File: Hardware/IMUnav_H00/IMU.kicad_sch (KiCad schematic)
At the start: 11 parts, among them U10 ADIS16505-2BMLZ, U8 MPU-6050, U9 LSM303C

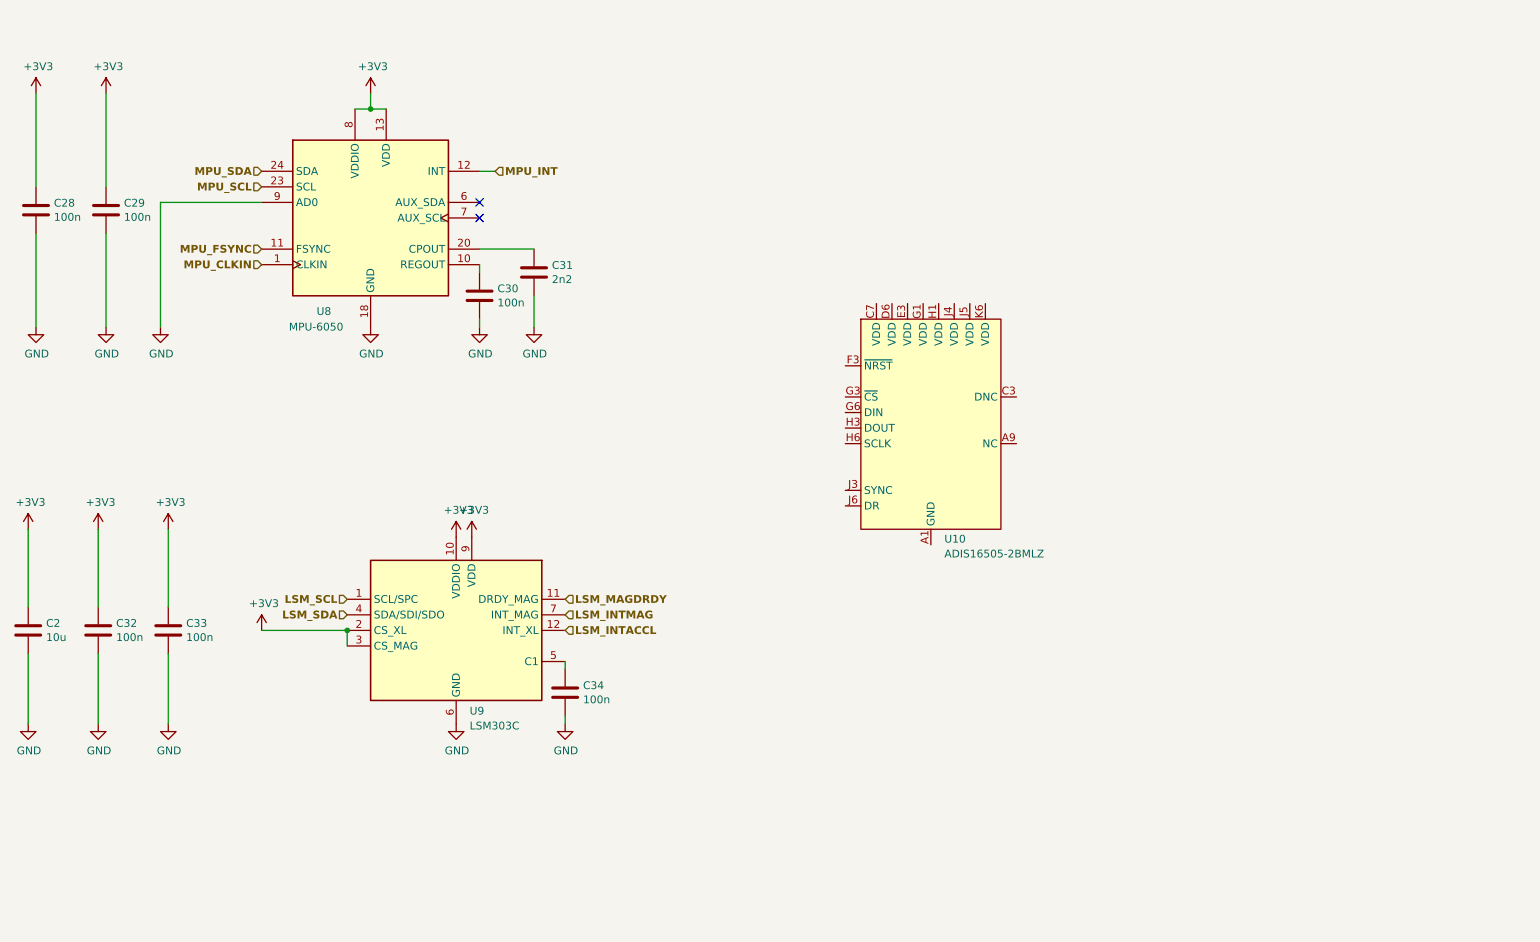
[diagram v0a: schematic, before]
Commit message: Added IMU connection, created symbol for ADIS16505 PCB version
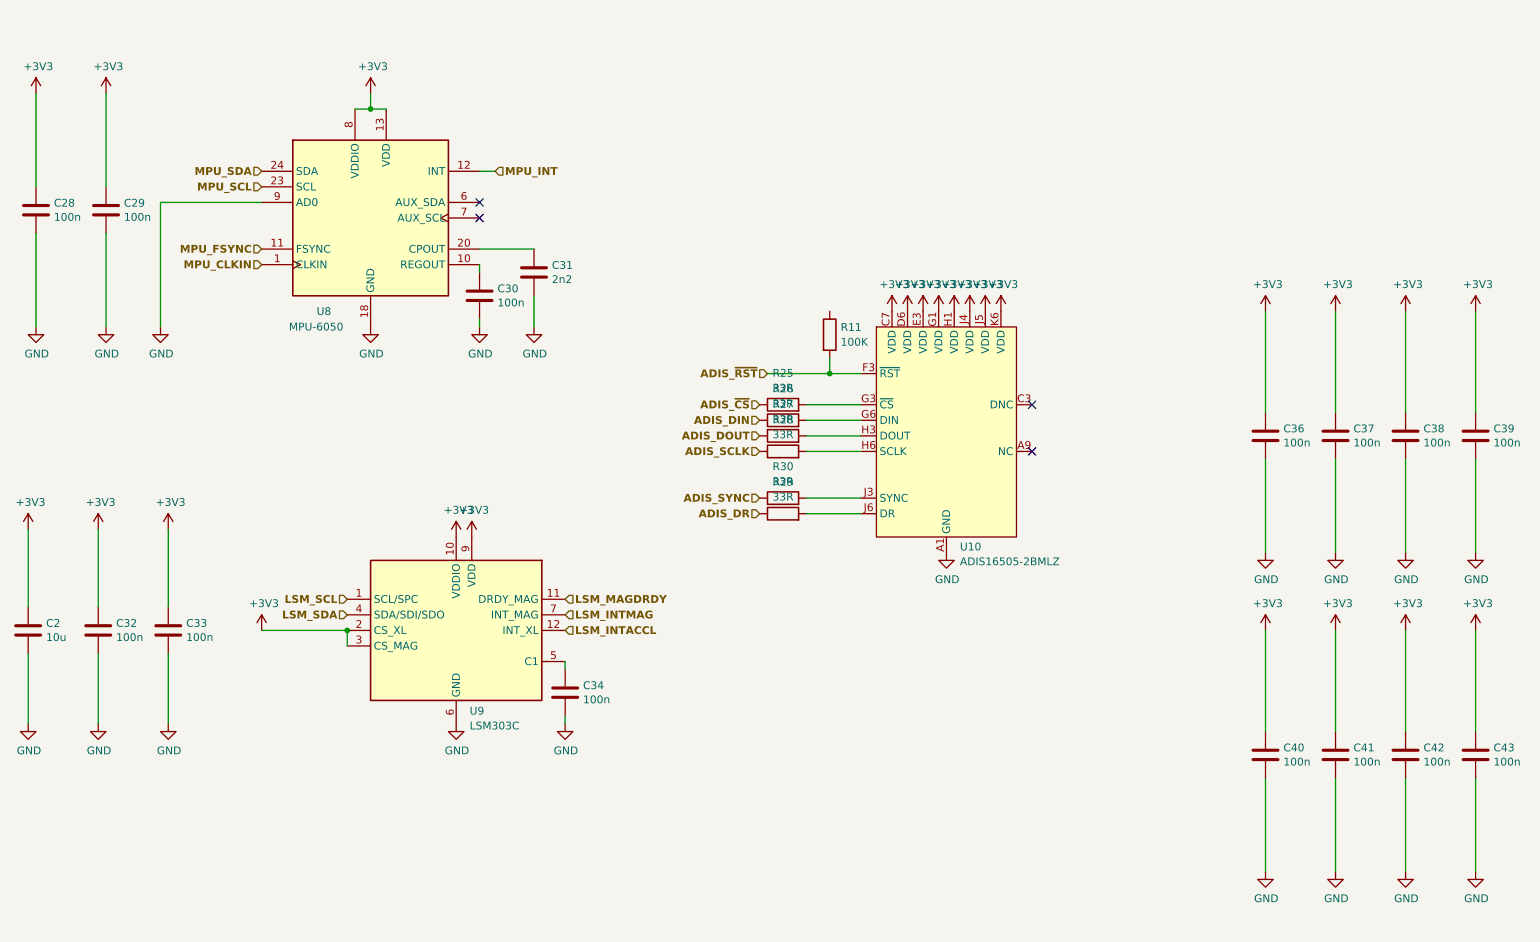
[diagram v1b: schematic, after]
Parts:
- added C36, C37, C38, C39, C40, C41, C42, C43: 100n, Capacitor_SMD:C_0603_1608Metric, symbol Device:C
- added R11: 100K, Resistor_SMD:R_0603_1608Metric, symbol Device:R
- added R25, R26, R27, R28, R29, R30: 33R, Resistor_SMD:R_0603_1608Metric, symbol Device:R
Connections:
- net +3V3: now also U10.C7 (VDD), U10.D6 (VDD), U10.E3 (VDD), U10.G1 (VDD), U10.H1 (VDD), U10.J4 (VDD), U10.J5 (VDD), U10.K6 (VDD), C36.1, C37.1, C38.1, C39.1, C40.1, C41.1, C42.1, C43.1
- net GND: now also U10.A1 (GND), U10.A2 (GND), U10.A3 (GND), U10.A4 (GND), U10.A5 (GND), U10.A6 (GND), U10.A7 (GND), U10.A8 (GND), U10.B3 (GND), U10.B4 (GND), U10.B5 (GND), U10.B6 (GND), U10.C2 (GND), U10.C6 (GND), U10.D3 (GND), U10.E2 (GND), U10.E6 (GND), U10.E7 (GND), U10.F1 (GND), U10.F5 (GND), U10.F6 (GND), U10.F8 (GND), U10.G2 (GND), U10.G7 (GND), U10.H8 (GND), U10.J2 (GND), U10.J7 (GND), U10.K1 (GND), U10.K3 (GND), U10.K8 (GND), C36.2, C37.2, C38.2, C39.2, C40.2, C41.2, C42.2, C43.2
- net ADIS_~{RST}: now reaches U10.F3 (~{RST})
- net ADIS_~{RST}: now also R11.2
- net at U10.G3 (~{CS}): now also R25.2
- net at U10.G6 (DIN): now also R26.2
- net at U10.H3 (DOUT): now also R27.2
- net at U10.H6 (SCLK): now also R28.2
- net at U10.J3 (SYNC): now also R30.2
- net at U10.J6 (DR): now also R29.2
- new net ADIS_DIN: R26.1
- new net ADIS_DOUT: R27.1
- new net ADIS_DR: R29.1
- new net ADIS_SCLK: R28.1
- new net ADIS_SYNC: R30.1
- new net ADIS_~{CS}: R25.1
- no-connect marks 2 -> 4
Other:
- moved on the sheet: U10

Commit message: Updated footprints, symbols and 3D models for ADIS165050 BGA and PCB variant
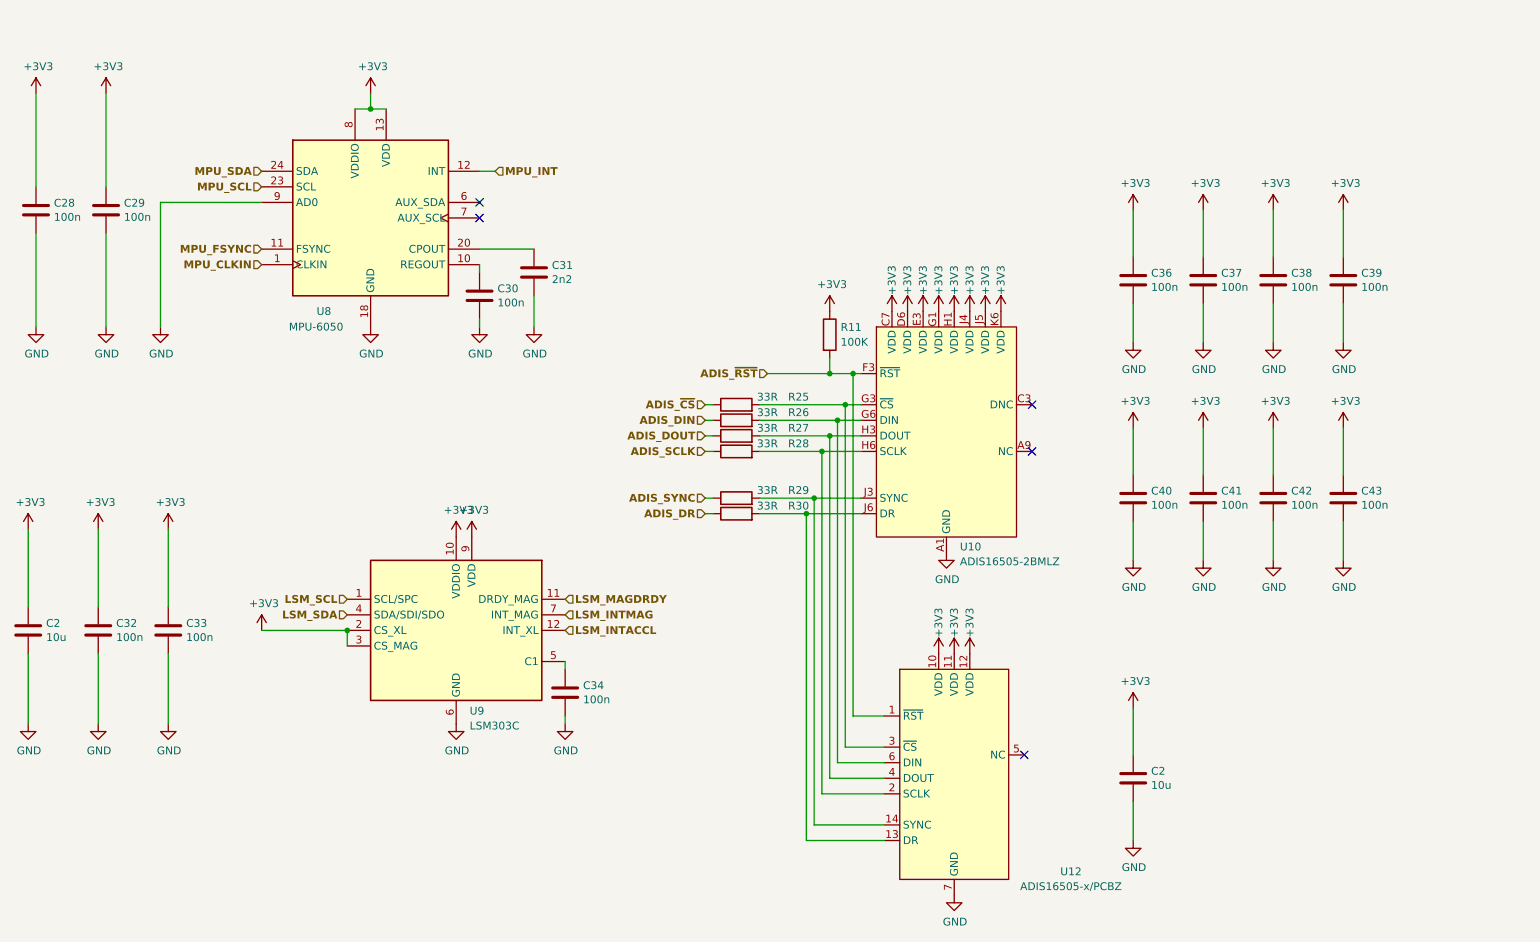
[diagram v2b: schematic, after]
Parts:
- added C2: 10u, Capacitor_SMD:C_0805_2012Metric, symbol Device:C
- added U12: ADIS16505-x/PCBZ, IMUnav:ADIS16505-PCBZ, symbol IMUnav:ADIS16505-PCB
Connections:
- net +3V3: now also R11.1, C2.1, U12.10 (VDD), U12.11 (VDD), U12.12 (VDD)
- net ADIS_DR: now also R30.1; no longer R29.1
- net ADIS_SYNC: now also R29.1; no longer R30.1
- net ADIS_~{RST}: now also U12.1 (~{RST})
- net GND: now also C2.2, U12.7 (GND), U12.8 (GND), U12.9 (GND)
- net at R28.2, U10.H6 (SCLK): now also U12.2 (SCLK)
- net at R27.2, U10.H3 (DOUT): now also U12.4 (DOUT)
- net at R26.2, U10.G6 (DIN): now also U12.6 (DIN)
- net at R25.2, U10.G3 (~{CS}): now also U12.3 (~{CS})
- net at R30.2: now also U10.J6 (DR), U12.13 (DR); no longer U10.J3 (SYNC)
- net at R29.2: now also U10.J3 (SYNC), U12.14 (SYNC); no longer U10.J6 (DR)
- new net: U12.15 (NC), U12.16 (NC), U12.5 (NC)
- no-connect marks 4 -> 5
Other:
- moved on the sheet: C36, C37, C38, C39, R25

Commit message: Added signal connections to MCU+misc
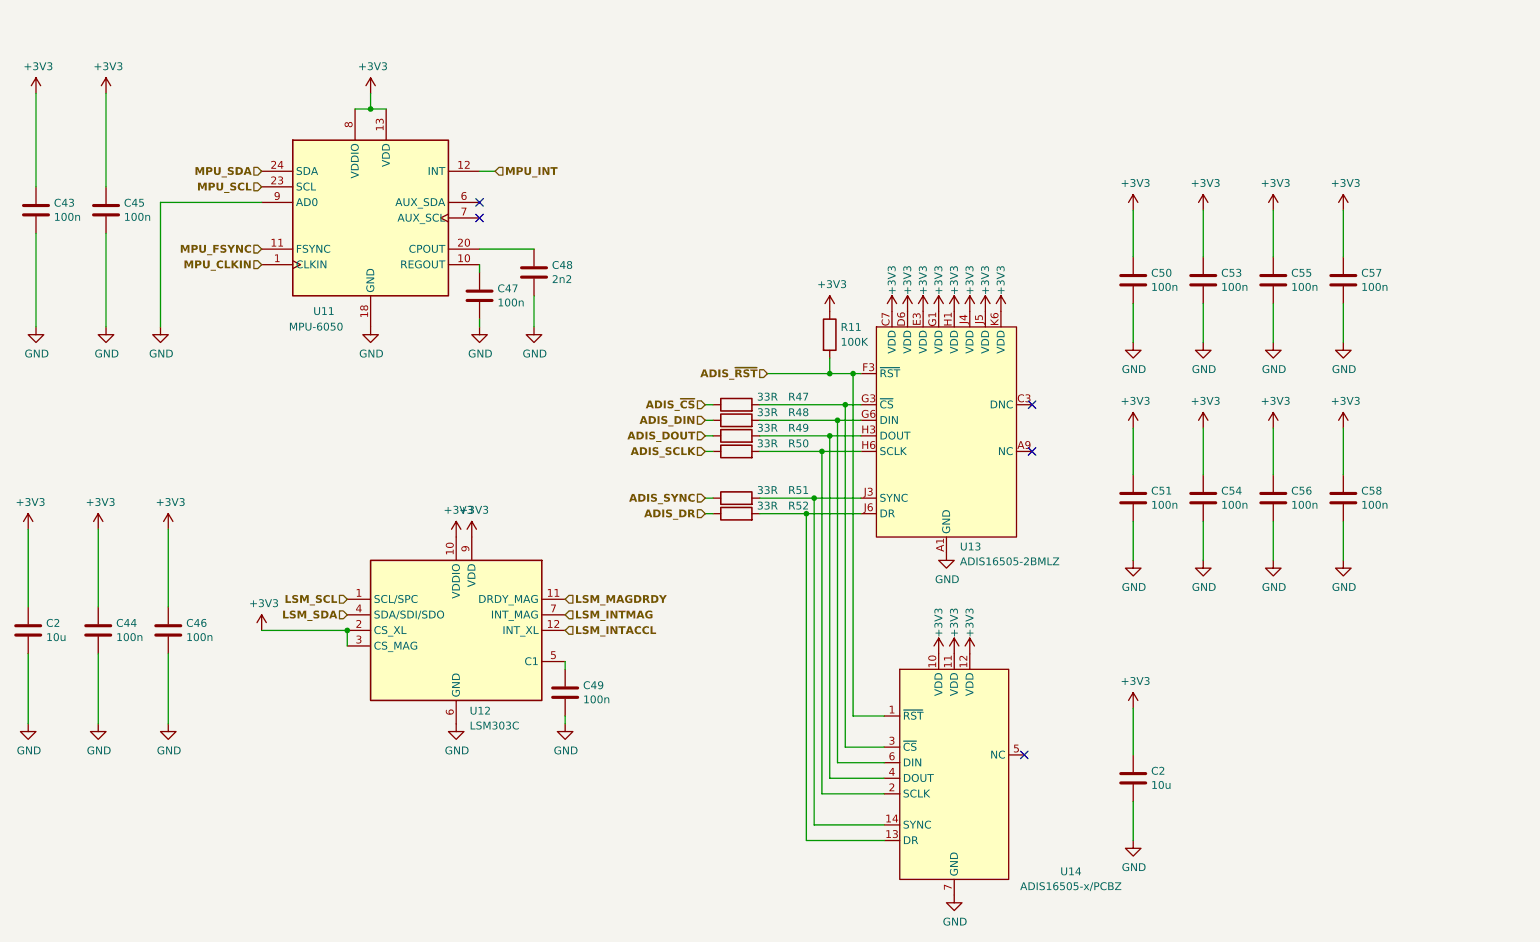
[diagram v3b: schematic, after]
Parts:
- renumbered C28 to C43, C32 to C44, C29 to C45, C33 to C46, C30 to C47, C31 to C48, C34 to C49, C36 to C50, C40 to C51, C37 to C53, C41 to C54, C38 to C55, C42 to C56, C39 to C57, C43 to C58, R25 to R47, R26 to R48, R27 to R49, R28 to R50, R29 to R51, R30 to R52, U8 to U11, U9 to U12, U10 to U13, U12 to U14

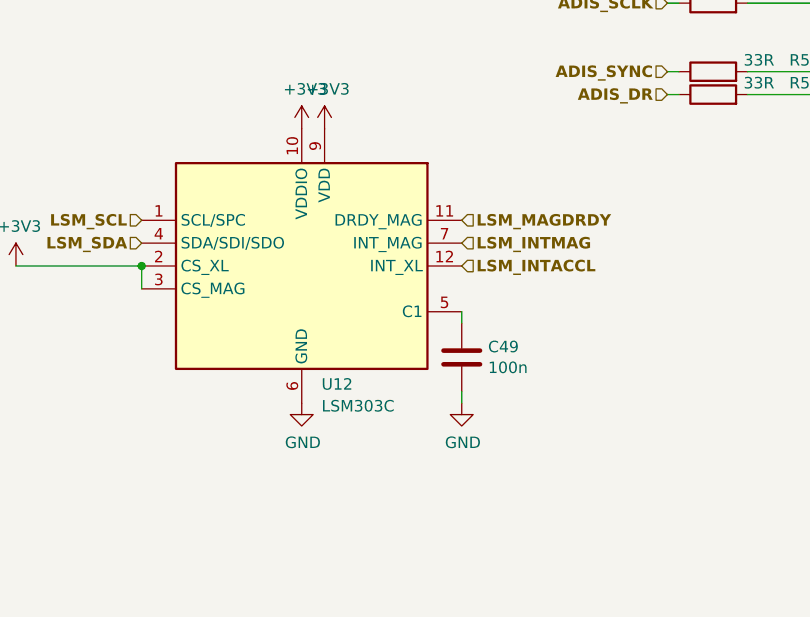
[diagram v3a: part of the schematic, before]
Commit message: Changed LSM303C to LSM303AGR
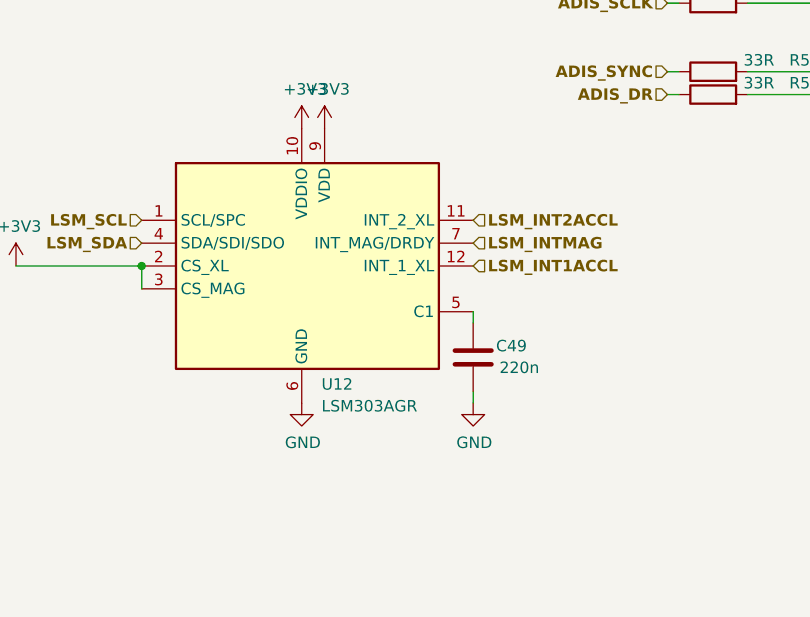
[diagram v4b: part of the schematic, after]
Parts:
- C49: value 100n -> 220n; LCSC C14663 -> C21120
- U12: value LSM303C -> LSM303AGR; LCSC (none) -> C126671
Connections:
- net LSM_INTACCL renamed LSM_INT1ACCL
- net LSM_MAGDRDY renamed LSM_INT2ACCL
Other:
- moved on the sheet: C49, U12
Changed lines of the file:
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@@
     (stroke (width 0) (type default))
   )
-  (wire (pts (xy 118.11 121.92) (xy 118.11 120.65))
+  (wire (pts (xy 119.38 121.92) (xy 119.38 120.65))
     (stroke (width 0) (type default))
   )
@@
     (stroke (width 0) (type default))
   )
-  (wire (pts (xy 118.11 129.54) (xy 118.11 130.81))
+  (wire (pts (xy 119.38 129.54) (xy 119.38 130.81))
     (stroke (width 0) (type default))
   )
@@
     (effects (font (size 1.27 1.27) (thickness 0.254) bold) (justify right))
   )
-  (hierarchical_label "LSM_INTACCL" (shape input) (at 118.11 115.57 0) (fields_autoplaced)
+  (hierarchical_label "LSM_INT1ACCL" (shape input) (at 119.38 115.57 0) (fields_autoplaced)
     (effects (font (size 1.27 1.27) (thickness 0.254) bold) (justify left))
   )
@@
     (effects (font (size 1.27 1.27) (thickness 0.254) bold) (justify right))
   )
-  (hierarchical_label "LSM_INTMAG" (shape input) (at 118.11 113.03 0) (fields_autoplaced)
+  (hierarchical_label "LSM_INTMAG" (shape input) (at 119.38 113.03 0) (fields_autoplaced)
     (effects (font (size 1.27 1.27) (thickness 0.254) bold) (justify left))
   )
@@
     (effects (font (size 1.27 1.27) (thickness 0.254) bold) (justify right))
   )
-  (hierarchical_label "LSM_MAGDRDY" (shape input) (at 118.11 110.49 0) (fields_autoplaced)
+  (hierarchical_label "LSM_INT2ACCL" (shape input) (at 119.38 110.49 0) (fields_autoplaced)
     (effects (font (size 1.27 1.27) (thickness 0.254) bold) (justify left))
   )
@@
     )
   )
-  (symbol (lib_id "power:GND") (at 118.11 130.81 0) (unit 1)
-    (in_bom yes) (on_board yes) (dnp no)
-    (property "Reference" "#PWR0154" (at 118.11 137.16 0)
-      (effects (font (size 1.27 1.27)) hide)
-    )
-    (property "Value" "GND" (at 118.237 135.2042 0)
-      (effects (font (size 1.27 1.27)))
-    )
-    (property "Footprint" "" (at 118.11 130.81 0)
-      (effects (font (size 1.27 1.27)) hide)
-    )
-    (property "Datasheet" "" (at 118.11 130.81 0)
+  (symbol (lib_id "power:GND") (at 119.38 130.81 0) (unit 1)
+    (in_bom yes) (on_board yes) (dnp no)
+    (property "Reference" "#PWR0154" (at 119.38 137.16 0)
+      (effects (font (size 1.27 1.27)) hide)
+    )
+    (property "Value" "GND" (at 119.507 135.2042 0)
+      (effects (font (size 1.27 1.27)))
+    )
+    (property "Footprint" "" (at 119.38 130.81 0)
+      (effects (font (size 1.27 1.27)) hide)
+    )
+    (property "Datasheet" "" (at 119.38 130.81 0)
       (effects (font (size 1.27 1.27)) hide)
     )
@@
       (effects (font (size 1.27 1.27)) (justify left))
     )
-    (property "Value" "LSM303C" (at 102.5241 131.1443 0)
+    (property "Value" "LSM303AGR" (at 102.5241 131.1443 0)
       (effects (font (size 1.27 1.27)) (justify left))
     )
@@
       (effects (font (size 1.27 1.27)) hide)
     )
-    (property "Datasheet" "www.st.com/resource/en/datasheet/lsm303c.pdf" (at 102.87 132.08 0)
+    (property "Datasheet" "https://www.st.com/resource/en/datasheet/lsm303agr.pdf" (at 102.87 132.08 0)
+      (effects (font (size 1.27 1.27)) hide)
+    )
+    (property "LCSC" "C126671" (at 100.33 115.57 0)
       (effects (font (size 1.27 1.27)) hide)
     )
@@
     )
   )
-  (symbol (lib_id "Device:C") (at 118.11 125.73 0) (unit 1)
-    (in_bom yes) (on_board yes) (dnp no)
-    (property "Reference" "C49" (at 121.031 124.5616 0)
+  (symbol (lib_id "Device:C") (at 119.38 125.73 0) (unit 1)
+    (in_bom yes) (on_board yes) (dnp no)
+    (property "Reference" "C49" (at 121.92 124.46 0)
       (effects (font (size 1.27 1.27)) (justify left))
     )
-    (property "Value" "100n" (at 121.031 126.873 0)
+    (property "Value" "220n" (at 122.301 126.873 0)
       (effects (font (size 1.27 1.27)) (justify left))
     )
-    (property "Footprint" "Capacitor_SMD:C_0603_1608Metric" (at 119.0752 129.54 0)
-      (effects (font (size 1.27 1.27)) hide)
-    )
-    (property "Datasheet" "~" (at 118.11 125.73 0)
-      (effects (font (size 1.27 1.27)) hide)
-    )
-    (property "LCSC" "C14663" (at 118.11 125.73 0)
-      (effects (font (size 1.27 1.27)) hide)
-    )
+    (property "Footprint" "Capacitor_SMD:C_0603_1608Metric" (at 120.3452 129.54 0)
+      (effects (font (size 1.27 1.27)) hide)
+    )
+    (property "Datasheet" "~" (at 119.38 125.73 0)
+      (effects (font (size 1.27 1.27)) hide)
+    )
+    (property "LCSC" "C21120" (at 119.38 125.73 0)
+      (effects (font (size 1.27 1.27)) hide)
+    )
